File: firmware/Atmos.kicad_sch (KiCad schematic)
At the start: 54 parts, among them J1 AS3935 breakout, J2 BME280 breakout, J3 USB_C_Receptacle_USB2.0_16P, J4 Micro_SD_Card, J5 Solar power input, J6 Conn_Coaxial, Q1 PMOS_Substrate, Q2 PMOS_Substrate, Q3 PMOS_Substrate, SW2 SW_Push, U1 ESP32-S3-WROOM-1, U10 TPS22918DBVR, U11 MAX17048G_T10, U12 CN3791, U13 SGP40-D-R4, U2 AP2112K-3.3, U3 DS3231M, U4 PMS5003, U5 LTC4412xS6, U7 RFM95W-915S2, U8 USBLC6-2SC6, U9 TPS61023DRLR

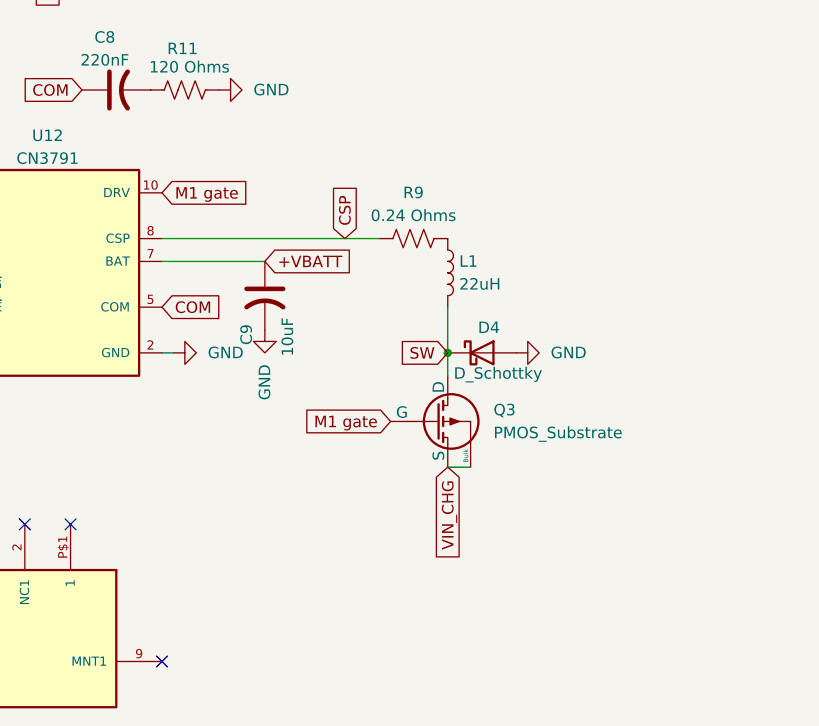
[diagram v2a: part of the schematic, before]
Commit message: fixed U12 wiring
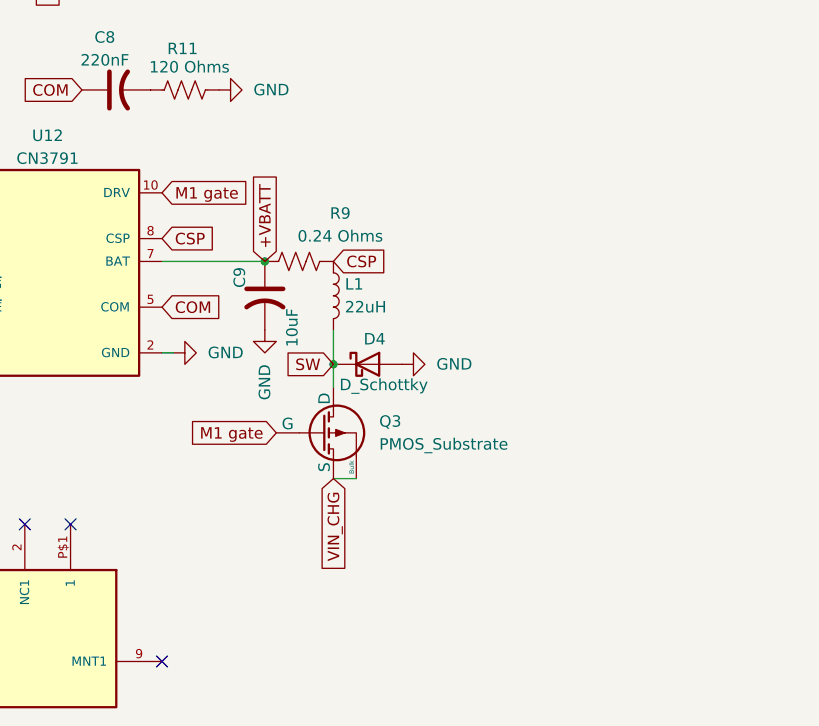
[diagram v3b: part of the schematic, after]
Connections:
- net +VBATT: now also R9.1
- net CSP: now also L1.1, R9.2; no longer R9.1
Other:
- moved on the sheet: D4, L1, Q3, R9
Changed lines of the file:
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@@
 	)
 	(junction
-		(at 160.02 157.48)
-		(diameter 0)
-		(color 0 0 0 0)
-	)
-	(junction
 		(at 29.21 57.15)
 		(diameter 0)
@@
 		(color 0 0 0 0)
 	)
+	(junction
+		(at 147.32 158.75)
+		(diameter 0)
+		(color 0 0 0 0)
+	)
+	(junction
+		(at 139.7 147.32)
+		(diameter 0)
+		(color 0 0 0 0)
+	)
 	(no_connect
 		(at 118.11 176.53)
@@
 	(wire
 		(pts
-			(xy 160.02 170.18) (xy 162.56 170.18)
+			(xy 147.32 171.45) (xy 149.86 171.45)
 		)
 		(stroke
@@
 	(wire
 		(pts
-			(xy 160.02 152.4) (xy 160.02 157.48)
-		)
-		(stroke
-			(width 0)
-			(type default)
-		)
-	)
-	(wire
-		(pts
 			(xy 101.6 152.4) (xy 102.87 152.4)
 		)
@@
 	(wire
 		(pts
-			(xy 213.36 76.2) (xy 220.98 76.2)
+			(xy 147.32 154.94) (xy 147.32 158.75)
 		)
 		(stroke
@@
 	(wire
 		(pts
-			(xy 134.62 -16.51) (xy 137.16 -16.51)
+			(xy 213.36 76.2) (xy 220.98 76.2)
 		)
 		(stroke
@@
 	(wire
 		(pts
-			(xy 29.21 57.15) (xy 29.21 59.69)
+			(xy 134.62 -16.51) (xy 137.16 -16.51)
 		)
 		(stroke
@@
 	(wire
 		(pts
-			(xy 128.27 144.78) (xy 152.4 144.78)
+			(xy 29.21 57.15) (xy 29.21 59.69)
 		)
 		(stroke
@@
 	(wire
 		(pts
-			(xy 160.02 157.48) (xy 160.02 160.02)
+			(xy 147.32 158.75) (xy 147.32 161.29)
 		)
 		(stroke
@@
 		)
 	)
+	(global_label "CSP"
+		(shape input)
+		(at 128.27 144.78 0)
+		(effects
+			(font
+				(size 1.27 1.27)
+			)
+			(justify left)
+		)
+		(property "Intersheetrefs" "${INTERSHEET_REFS}"
+			(at 155.3247 144.78 0)
+			(effects
+				(font
+					(size 1.27 1.27)
+				)
+				(justify left)
+				(hide yes)
+			)
+		)
+	)
 	(global_label "+VBATT"
 		(shape input)
-		(at 139.7 147.32 0)
+		(at 139.7 147.32 90)
 		(fields_autoplaced yes)
 		(effects
@@
 		)
 		(property "Intersheetrefs" "${INTERSHEET_REFS}"
-			(at 149.64 147.32 0)
+			(at 139.7 137.38 90)
 			(effects
 				(font
@@
 		)
 	)
+	(global_label "CSP"
+		(shape input)
+		(at 147.32 147.32 0)
+		(effects
+			(font
+				(size 1.27 1.27)
+			)
+			(justify left)
+		)
+		(property "Intersheetrefs" "${INTERSHEET_REFS}"
+			(at 174.3747 147.32 0)
+			(effects
+				(font
+					(size 1.27 1.27)
+				)
+				(justify left)
+				(hide yes)
+			)
+		)
+	)
 	(global_label "+3V3"
 		(shape input)
@@
 		)
 	)
-	(global_label "CSP"
-		(shape input)
-		(at 148.59 144.78 90)
-		(effects
-			(font
-				(size 1.27 1.27)
-			)
-			(justify left)
-		)
-		(property "Intersheetrefs" "${INTERSHEET_REFS}"
-			(at 148.59 117.7253 90)
-			(effects
-				(font
-					(size 1.27 1.27)
-				)
-				(justify left)
-				(hide yes)
-			)
-		)
-	)
 	(global_label "VIN_CHG"
 		(shape input)
@@
 	(global_label "VIN_CHG"
 		(shape input)
-		(at 160.02 170.18 270)
+		(at 147.32 171.45 270)
 		(fields_autoplaced yes)
 		(effects
@@
 		)
 		(property "Intersheetrefs" "${INTERSHEET_REFS}"
-			(at 160.02 181.0272 90)
+			(at 147.32 182.2972 90)
 			(effects
 				(font
@@
 	(global_label "SW"
 		(shape input)
-		(at 160.02 157.48 180)
+		(at 147.32 158.75 180)
 		(fields_autoplaced yes)
 		(effects
@@
 		)
 		(property "Intersheetrefs" "${INTERSHEET_REFS}"
-			(at 154.3739 157.48 0)
+			(at 141.6739 158.75 0)
 			(effects
 				(font
@@
 	(global_label "M1 gate"
 		(shape input)
-		(at 153.67 165.1 180)
+		(at 140.97 166.37 180)
 		(fields_autoplaced yes)
 		(effects
@@
 		)
 		(property "Intersheetrefs" "${INTERSHEET_REFS}"
-			(at 142.944 165.1 0)
+			(at 130.244 166.37 0)
 			(effects
 				(font
@@
 	(symbol
 		(lib_id "Device:R_US")
-		(at 156.21 144.78 90)
+		(at 143.51 147.32 90)
 		(unit 1)
 		(exclude_from_sim no)
@@
 		(dnp no)
 		(property "Reference" "R9"
-			(at 156.21 139.7 90)
+			(at 148.082 141.986 90)
 			(effects
 				(font
@@
 		)
 		(property "Value" "0.24 Ohms"
-			(at 156.21 142.24 90)
+			(at 148.082 144.526 90)
 			(effects
 				(font
@@
 		)
 		(property "Footprint" ""
-			(at 156.464 143.764 90)
+			(at 143.764 146.304 90)
 			(effects
 				(font
@@
 		)
 		(property "Datasheet" "~"
-			(at 156.21 144.78 0)
+			(at 143.51 147.32 0)
 			(effects
 				(font
@@
 		)
 		(property "Description" "Resistor, US symbol"
-			(at 156.21 144.78 0)
+			(at 143.51 147.32 0)
 			(effects
 				(font
@@
 		)
 		(instances
-			(project ""
+			(project "Atmos"
 				(path "/821c823f-0cdf-48e4-87e1-02b442913dca"
 					(reference "R9")
@@
 	(symbol
 		(lib_id "Device:L")
-		(at 160.02 148.59 0)
+		(at 147.32 151.13 0)
 		(unit 1)
 		(exclude_from_sim no)
@@
 		(fields_autoplaced yes)
 		(property "Reference" "L1"
-			(at 161.29 147.3199 0)
+			(at 148.59 149.8599 0)
 			(effects
 				(font
@@
 		)
 		(property "Value" "22uH"
-			(at 161.29 149.8599 0)
+			(at 148.59 152.3999 0)
 			(effects
 				(font
@@
 		)
 		(property "Footprint" ""
-			(at 160.02 148.59 0)
+			(at 147.32 151.13 0)
 			(effects
 				(font
@@
 		)
 		(property "Datasheet" "~"
-			(at 160.02 148.59 0)
+			(at 147.32 151.13 0)
 			(effects
 				(font
@@
 		)
 		(property "Description" "Inductor"
-			(at 160.02 148.59 0)
+			(at 147.32 151.13 0)
 			(effects
 				(font
@@
 		(dnp no)
 		(property "Reference" "C9"
-			(at 137.668 155.448 90)
+			(at 136.906 149.098 90)
 			(effects
 				(font
@@
 		)
 		(property "Value" "10uF"
-			(at 142.24 155.702 90)
+			(at 142.748 154.686 90)
 			(effects
 				(font
@@
 	(symbol
 		(lib_id "Simulation_SPICE:PMOS_Substrate")
-		(at 157.48 165.1 0)
+		(at 144.78 166.37 0)
 		(unit 1)
 		(exclude_from_sim no)
@@
 		(fields_autoplaced yes)
 		(property "Reference" "Q3"
-			(at 165.1 163.8299 0)
+			(at 152.4 165.0999 0)
 			(effects
 				(font
@@
 		)
 		(property "Value" "PMOS_Substrate"
-			(at 165.1 166.3699 0)
+			(at 152.4 167.6399 0)
 			(effects
 				(font
@@
 		)
 		(property "Footprint" ""
-			(at 198.12 165.1 0)
+			(at 185.42 166.37 0)
 			(effects
 				(font
@@
 		)
 		(property "Datasheet" "https://ngspice.sourceforge.io/docs/ngspice-html-manual/manual.xhtml#cha_MOSFETs"
-			(at 157.48 182.88 0)
+			(at 144.78 184.15 0)
 			(effects
 				(font
@@
 		)
 		(property "Description" "P-channel MOSFET symbol with substrate (bulk) pin"
-			(at 157.48 165.1 0)
+			(at 144.78 166.37 0)
 			(effects
 				(font
@@
 		)
 		(property "Sim.Device" "PMOS"
-			(at 157.48 179.07 0)
+			(at 144.78 180.34 0)
 			(effects
 				(font
@@
 		)
 		(property "Sim.Type" "MOS1"
-			(at 157.48 180.975 0)
+			(at 144.78 182.245 0)
 			(effects
 				(font
@@
 		)
 		(property "Sim.Pins" "1=D 2=G 3=S 4=B"
-			(at 157.48 177.165 0)
+			(at 144.78 178.435 0)
 			(effects
 				(font
@@
 	(symbol
 		(lib_id "power:GND")
-		(at 167.64 157.48 90)
+		(at 154.94 158.75 90)
 		(unit 1)
 		(exclude_from_sim no)
@@
 		(fields_autoplaced yes)
 		(property "Reference" "#PWR029"
-			(at 173.99 157.48 0)
+			(at 161.29 158.75 0)
 			(effects
 				(font
@@
 		)
 		(property "Value" "GND"
-			(at 171.457 157.4799 90)
+			(at 158.757 158.7499 90)
 			(effects
 				(font
@@
 		)
 		(property "Footprint" ""
-			(at 167.64 157.48 0)
+			(at 154.94 158.75 0)
 			(effects
 				(font
@@
 		)
 		(property "Datasheet" ""
-			(at 167.64 157.48 0)
+			(at 154.94 158.75 0)
 			(effects
 				(font
@@
 		)
 		(property "Description" "Power symbol creates a global label with name \"GND\" , ground"
-			(at 167.64 157.48 0)
+			(at 154.94 158.75 0)
 			(effects
 				(font
@@
 	(symbol
 		(lib_id "Device:D_Schottky")
-		(at 163.83 157.48 0)
+		(at 151.13 158.75 0)
 		(unit 1)
 		(exclude_from_sim no)
@@
 		(dnp no)
 		(property "Reference" "D4"
-			(at 164.592 154.686 0)
+			(at 151.892 155.956 0)
 			(effects
 				(font
@@
 		)
 		(property "Value" "D_Schottky"
-			(at 165.608 159.766 0)
+			(at 152.908 161.036 0)
 			(effects
 				(font
@@
 		)
 		(property "Footprint" ""
-			(at 163.83 157.48 0)
+			(at 151.13 158.75 0)
 			(effects
 				(font
@@
 		)
 		(property "Datasheet" "~"
-			(at 163.83 157.48 0)
+			(at 151.13 158.75 0)
 			(effects
 				(font
@@
 		)
 		(property "Description" "Schottky diode"
-			(at 163.83 157.48 0)
+			(at 151.13 158.75 0)
 			(effects
 				(font

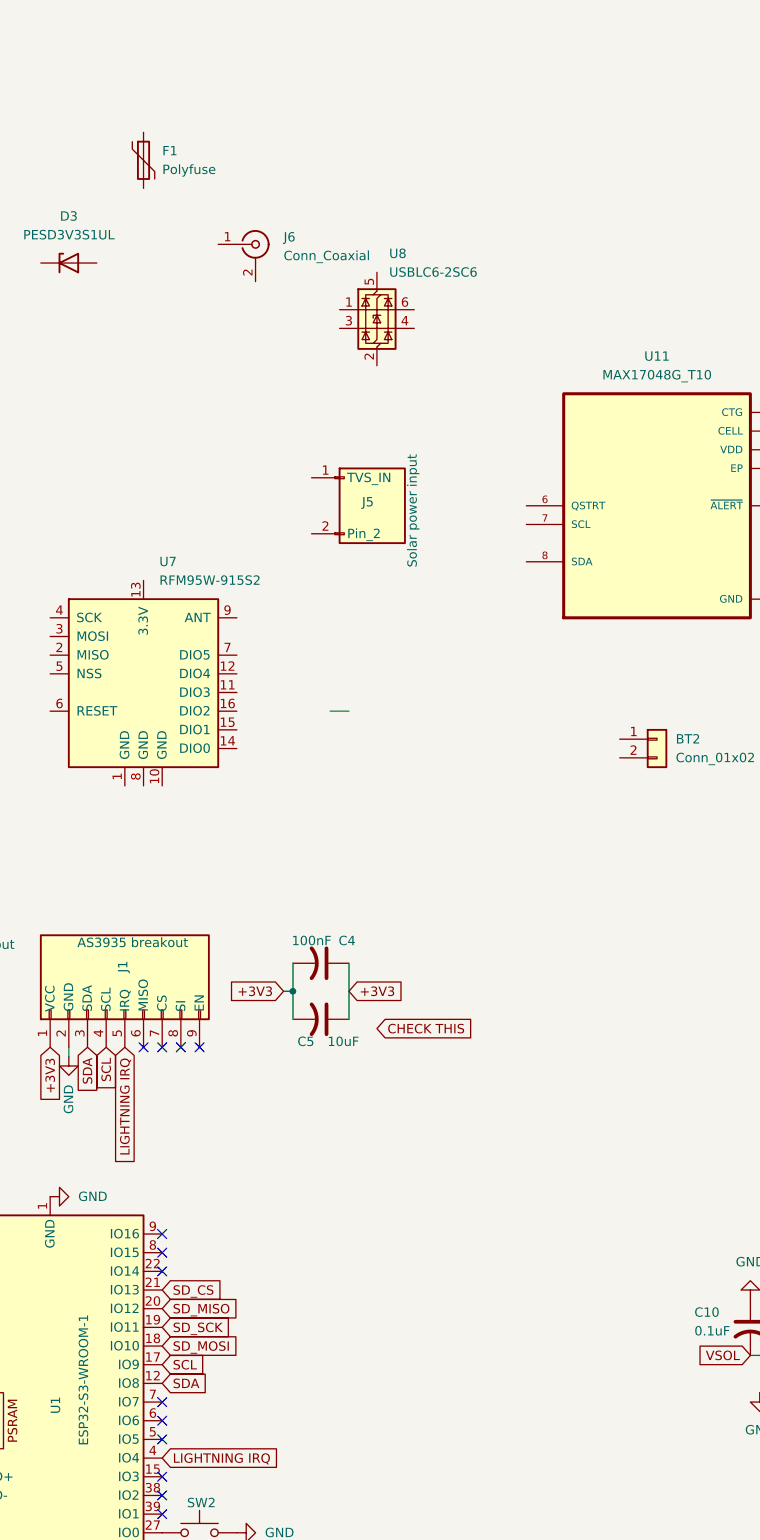
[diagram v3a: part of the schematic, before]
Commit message: wired J5 solar
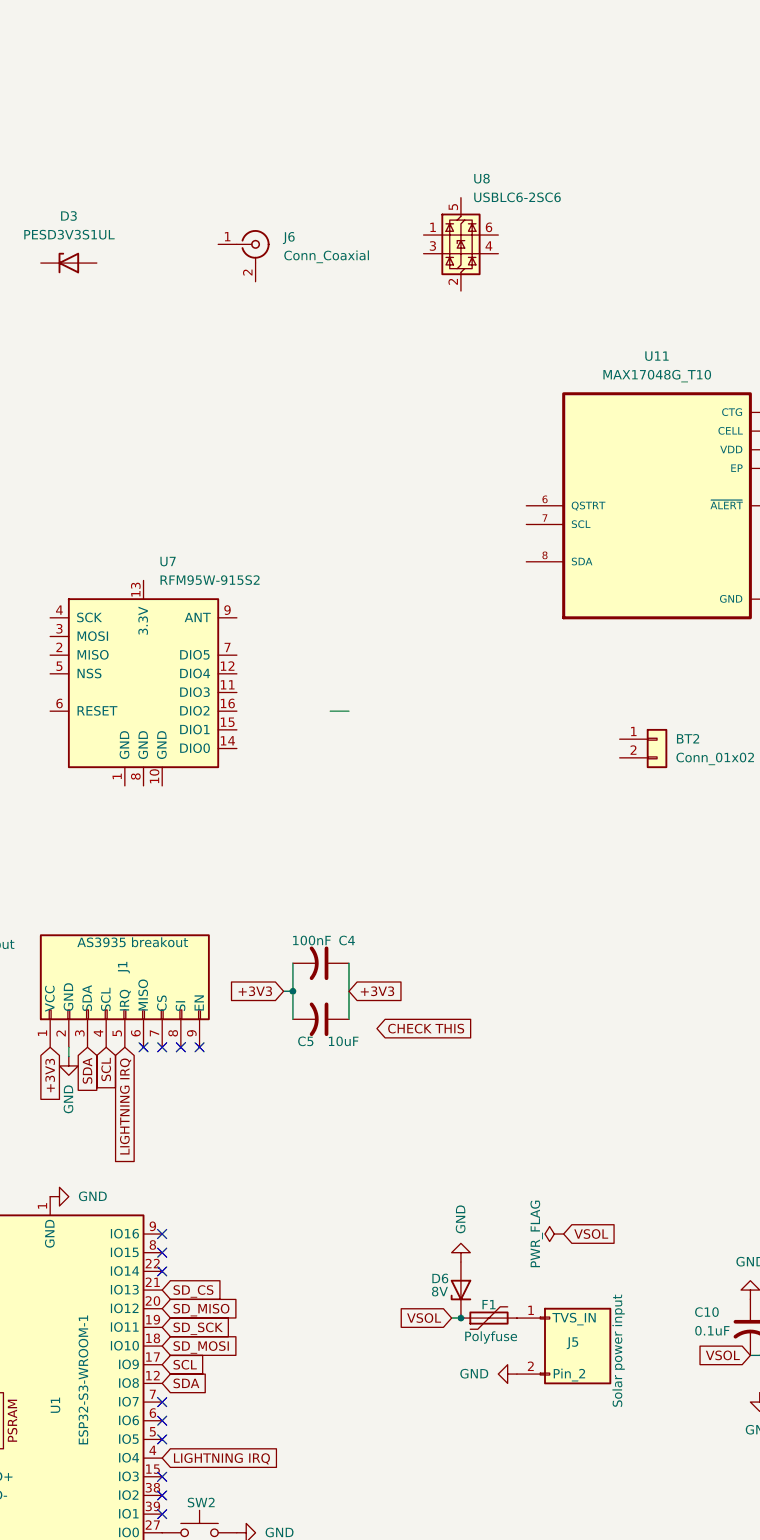
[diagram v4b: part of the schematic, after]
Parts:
- added D6: 8V, symbol Device:D_Zener
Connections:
- net GND: now also J5.2 (Pin_2), D6.2 (A)
- net VSOL: now also F1.1, D6.1 (K)
- net at J5.1 (TVS_IN): now also F1.2
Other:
- moved on the sheet: F1, J5, U8

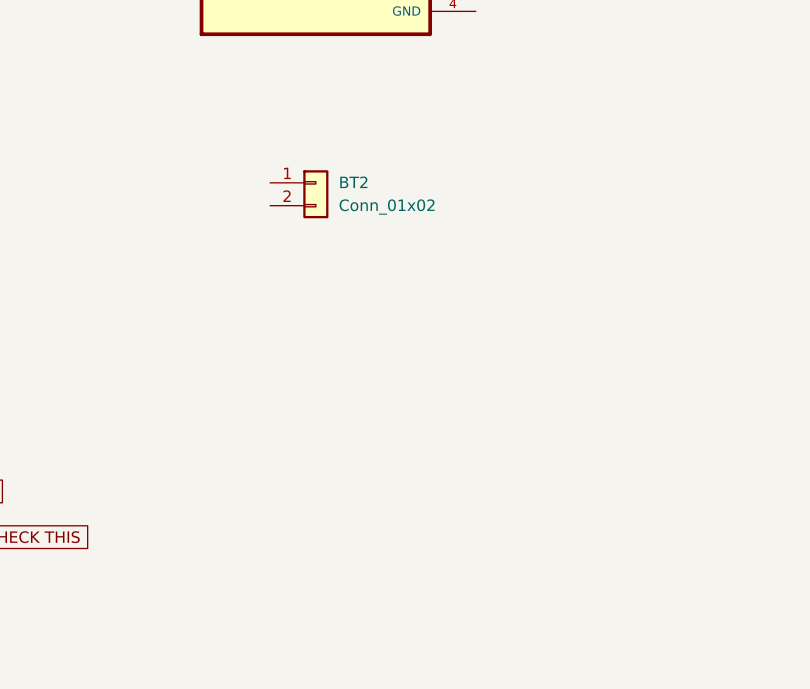
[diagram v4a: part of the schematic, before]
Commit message: BT2 wired
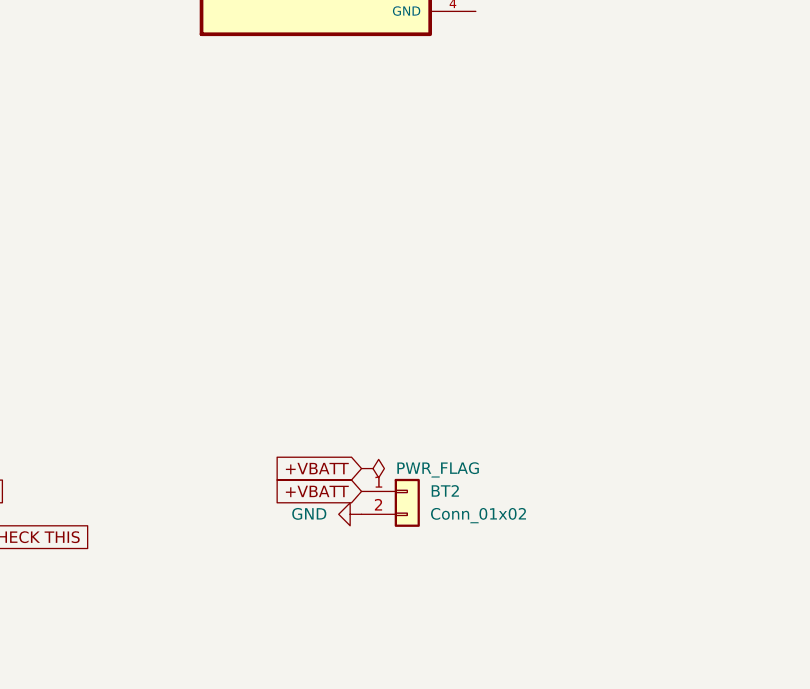
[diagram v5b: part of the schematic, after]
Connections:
- net +VBATT: now also BT2.1 (Pin_1)
- net GND: now also BT2.2 (Pin_2)
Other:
- moved on the sheet: BT2
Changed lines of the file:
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@@
 		)
 	)
+	(global_label "+VBATT"
+		(shape input)
+		(at 184.15 21.59 180)
+		(fields_autoplaced yes)
+		(effects
+			(font
+				(size 1.27 1.27)
+			)
+			(justify right)
+		)
+		(property "Intersheetrefs" "${INTERSHEET_REFS}"
+			(at 174.21 21.59 0)
+			(effects
+				(font
+					(size 1.27 1.27)
+				)
+				(justify right)
+				(hide yes)
+			)
+		)
+	)
 	(global_label "VIN_CHG"
 		(shape input)
@@
 		)
 	)
+	(global_label "+VBATT"
+		(shape input)
+		(at 184.15 19.05 180)
+		(fields_autoplaced yes)
+		(effects
+			(font
+				(size 1.27 1.27)
+			)
+			(justify right)
+		)
+		(property "Intersheetrefs" "${INTERSHEET_REFS}"
+			(at 174.21 19.05 0)
+			(effects
+				(font
+					(size 1.27 1.27)
+				)
+				(justify right)
+				(hide yes)
+			)
+		)
+	)
 	(global_label "VBUS"
 		(shape input)
@@
 	)
 	(symbol
+		(lib_id "power:PWR_FLAG")
+		(at 184.15 19.05 270)
+		(unit 1)
+		(exclude_from_sim no)
+		(in_bom yes)
+		(on_board yes)
+		(dnp no)
+		(fields_autoplaced yes)
+		(property "Reference" "#FLG05"
+			(at 186.055 19.05 0)
+			(effects
+				(font
+					(size 1.27 1.27)
+				)
+				(hide yes)
+			)
+		)
+		(property "Value" "PWR_FLAG"
+			(at 187.96 19.0499 90)
+			(effects
+				(font
+					(size 1.27 1.27)
+				)
+				(justify left)
+			)
+		)
+		(property "Footprint" ""
+			(at 184.15 19.05 0)
+			(effects
+				(font
+					(size 1.27 1.27)
+				)
+				(hide yes)
+			)
+		)
+		(property "Datasheet" "~"
+			(at 184.15 19.05 0)
+			(effects
+				(font
+					(size 1.27 1.27)
+				)
+				(hide yes)
+			)
+		)
+		(property "Description" "Special symbol for telling ERC where power comes from"
+			(at 184.15 19.05 0)
+			(effects
+				(font
+					(size 1.27 1.27)
+				)
+				(hide yes)
+			)
+		)
+		(pin "1"
+		)
+		(instances
+			(project ""
+				(path "/821c823f-0cdf-48e4-87e1-02b442913dca"
+					(reference "#FLG05")
+					(unit 1)
+				)
+			)
+		)
+	)
+	(symbol
 		(lib_id "power:GND")
 		(at 119.38 100.33 90)
@@
 	(symbol
 		(lib_id "Connector_Generic:Conn_01x02")
-		(at 179.07 -12.7 0)
+		(at 189.23 21.59 0)
 		(unit 1)
 		(exclude_from_sim no)
@@
 		(fields_autoplaced yes)
 		(property "Reference" "BT2"
-			(at 181.61 -12.7001 0)
+			(at 191.77 21.5899 0)
 			(effects
 				(font
@@
 		)
 		(property "Value" "Conn_01x02"
-			(at 181.61 -10.1601 0)
+			(at 191.77 24.1299 0)
 			(effects
 				(font
@@
 		)
 		(property "Footprint" ""
-			(at 179.07 -12.7 0)
+			(at 189.23 21.59 0)
 			(effects
 				(font
@@
 		)
 		(property "Datasheet" "~"
-			(at 179.07 -12.7 0)
+			(at 189.23 21.59 0)
 			(effects
 				(font
@@
 		)
 		(property "Description" "Generic connector, single row, 01x02, script generated (kicad-library-utils/schlib/autogen/connector/)"
-			(at 179.07 -12.7 0)
+			(at 189.23 21.59 0)
 			(effects
 				(font
@@
 					(unit 1)
 				)
+			)
+		)
+	)
+	(symbol
+		(lib_id "power:GND")
+		(at 184.15 24.13 270)
+		(unit 1)
+		(exclude_from_sim no)
+		(in_bom yes)
+		(on_board yes)
+		(dnp no)
+		(fields_autoplaced yes)
+		(property "Reference" "#PWR034"
+			(at 177.8 24.13 0)
+			(effects
+				(font
+					(size 1.27 1.27)
+				)
+				(hide yes)
+			)
+		)
+		(property "Value" "GND"
+			(at 180.34 24.1299 90)
+			(effects
+				(font
+					(size 1.27 1.27)
+				)
+				(justify right)
+			)
+		)
+		(property "Footprint" ""
+			(at 184.15 24.13 0)
+			(effects
+				(font
+					(size 1.27 1.27)
+				)
+				(hide yes)
+			)
+		)
+		(property "Datasheet" ""
+			(at 184.15 24.13 0)
+			(effects
+				(font
+					(size 1.27 1.27)
+				)
+				(hide yes)
+			)
+		)
+		(property "Description" "Power symbol creates a global label with name \"GND\" , ground"
+			(at 184.15 24.13 0)
+			(effects
+				(font
+					(size 1.27 1.27)
+				)
+				(hide yes)
+			)
+		)
+		(pin "1"
+		)
+		(instances
+			(project ""
+				(path "/821c823f-0cdf-48e4-87e1-02b442913dca"
+					(reference "#PWR034")
+					(unit 1)
+				)
